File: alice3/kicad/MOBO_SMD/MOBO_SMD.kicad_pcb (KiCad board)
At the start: 2 copper layers, 90.2 x 48.3 mm, 64 parts, among them CON1 MicroSD, J1 VGA, P1 CONN_01X05, P2 USB_OTG, P3 UART1, SW1 RESET, SW2 SOFT RESET, SW3 FLASH ARM, U1 Z80CPU-SMD, U2 Propeller_P8X32A-Q44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

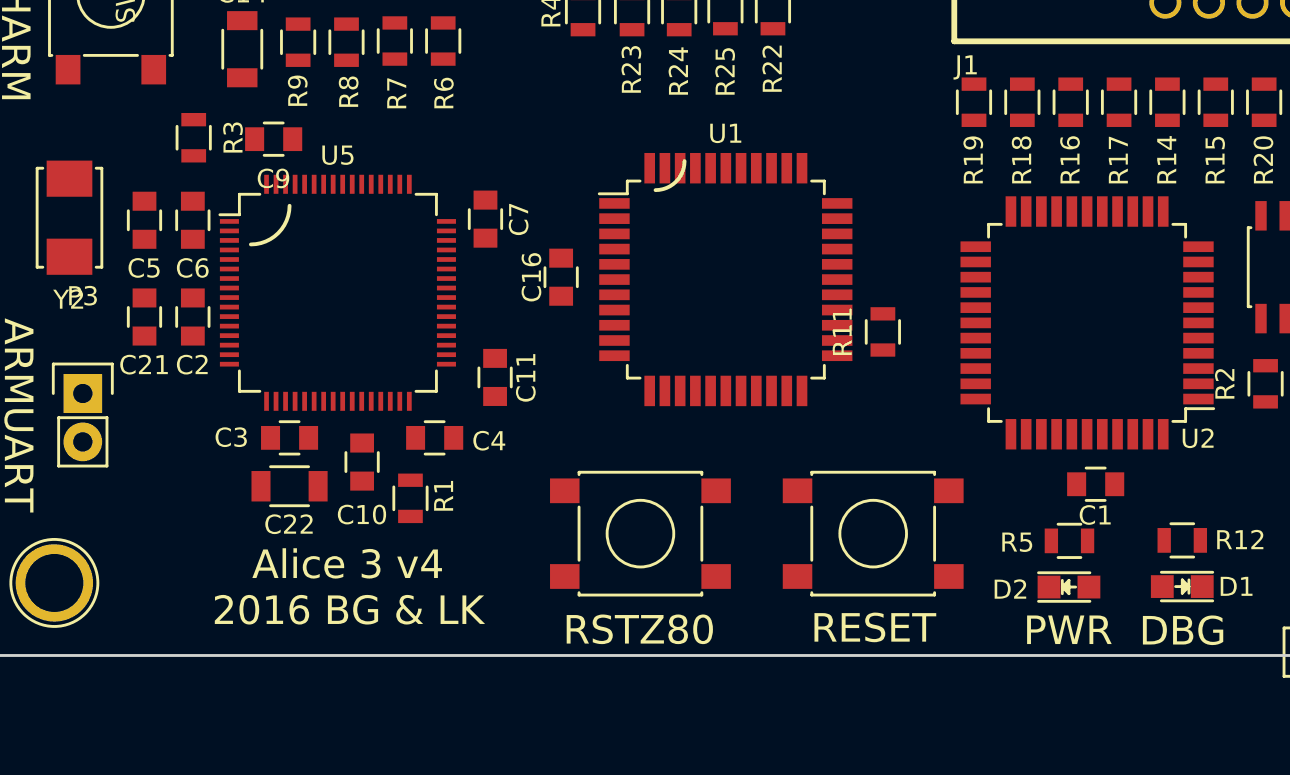
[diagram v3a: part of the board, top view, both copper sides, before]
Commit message: Fix microUSB and mounting holes
Fix footprint for microUSB

Give references for mounting holes
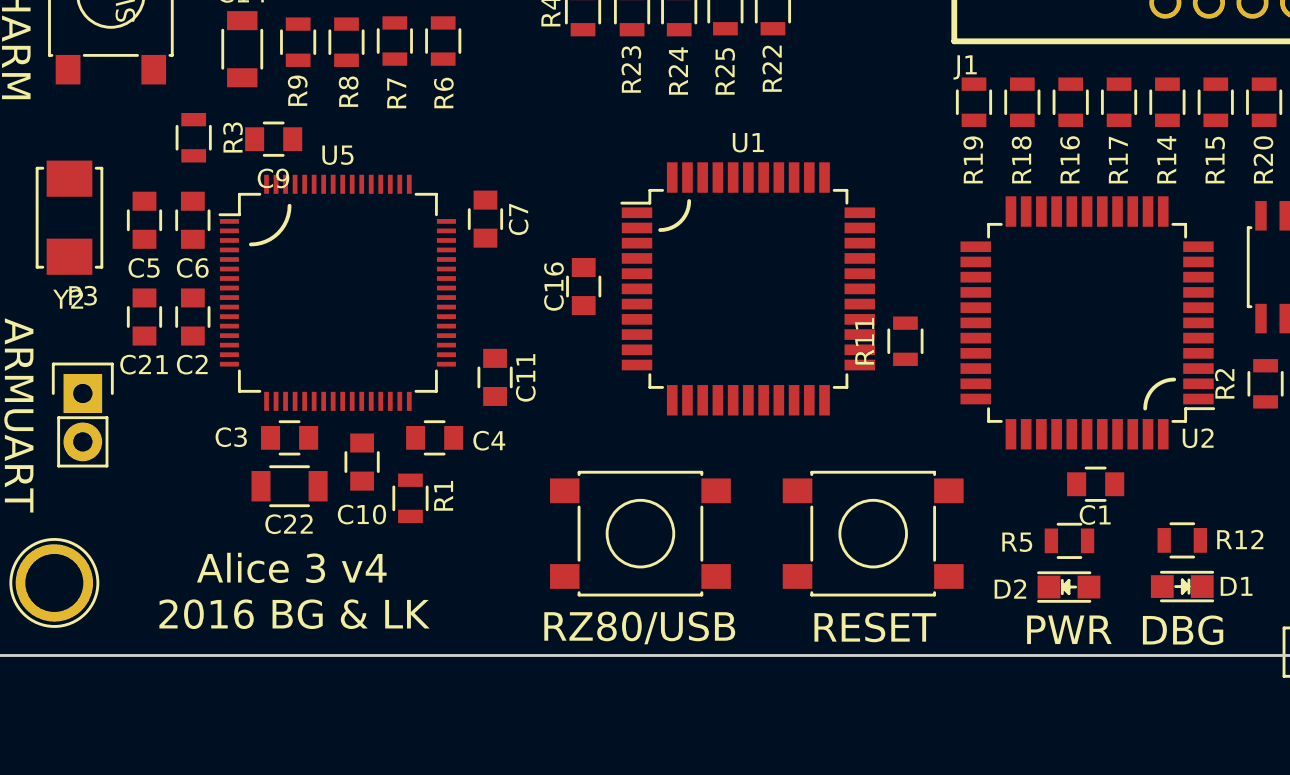
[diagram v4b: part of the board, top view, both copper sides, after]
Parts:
- moved C16 1.28 mm to (140.8, 102.5)
- moved R11 1.28 mm to (157.7, 105.4)
- moved U1 1.28 mm to (149.5, 102.7)
- renumbered REF** to HOLE0, REF** to HOLE1, REF** to HOLE2, REF** to HOLE3
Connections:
- U5 pad 10: ~WR -> A2
- U5 pad 11: A15 -> A3
- U5 pad 2: A10 -> A13
- U5 pad 24: A7 -> A4
- U5 pad 25: A2 -> A5
- U5 pad 26: ~Z80_RESET -> ~IORQ
- U5 pad 29: A4 -> ~BUSRQ
- U5 pad 3: ~PROP_READY~ -> A14
- U5 pad 37: A14 -> A6
- U5 pad 38: A13 -> A7
- U5 pad 39: A12 -> A8
- U5 pad 4: ~RFSH -> A15
- U5 pad 40: A8 -> A9
- U5 pad 46: A1 -> ~PROP_READY~
- U5 pad 49: A0 -> ~RFSH
- U5 pad 51: ~BUSACK -> A10
- U5 pad 52: ~BUSRQ -> A11
- U5 pad 53: A11 -> A12
- U5 pad 55: A3 -> ~RD
- U5 pad 56: A9 -> ~WR
- U5 pad 61: A6 -> ~Z80_RESET
- U5 pad 62: A5 -> ~BUSACK
- U5 pad 8: ~IORQ -> A0
- U5 pad 9: ~RD -> A1
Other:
- board text added: "RZ80/USB"
- board text removed: "RSTZ80"
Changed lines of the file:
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@@
 (kicad_pcb (version 4) (host pcbnew 4.0.6)
   (general
-    (links 218)
-    (no_connects 218)
+    (links 220)
+    (no_connects 220)
     (area 109.144999 73.584999 199.465001 121.995001)
     (thickness 1.6)
-    (drawings 16)
+    (drawings 17)
     (tracks 0)
     (zones 0)
@@
   )
   (module Housings_QFP:LQFP-44_10x10mm_Pitch0.8mm (layer F.Cu)
-    (at 148.3 102.175)
+    (at 149.484423 102.664503)
     (descr "LQFP44 (see Appnote_PCB_Guidelines_TRINAMIC_packages.pdf)")
     (tags "QFP 0.8")
@@
   )
   (module Capacitors_SMD:C_0805 (layer F.Cu)
-    (at 139.65 102.05 270)
+    (at 140.834423 102.539503 270)
     (descr "Capacitor SMD 0805, reflow soldering, AVX (see smccp.pdf)")
     (tags "capacitor 0805")
@@
   )
   (module Resistors_SMD:R_0805 (layer F.Cu)
-    (at 156.55 104.925 90)
+    (at 157.734423 105.414503 90)
     (descr "Resistor SMD 0805, reflow soldering, Vishay (see dcrcw.pdf)")
     (tags "resistor 0805")
@@
     (descr "module 1 pin (ou trou mecanique de percage)")
     (tags DEV)
-    (fp_text reference REF** (at 0 -3.048) (layer F.SilkS) hide
+    (fp_text reference HOLE0 (at 0 -3.048) (layer F.SilkS) hide
       (effects (font (size 1 1) (thickness 0.15)))
     )
@@
     (descr "module 1 pin (ou trou mecanique de percage)")
     (tags DEV)
-    (fp_text reference REF** (at 0 -3.048) (layer F.SilkS) hide
+    (fp_text reference HOLE1 (at 0 -3.048) (layer F.SilkS) hide
       (effects (font (size 1 1) (thickness 0.15)))
     )
@@
     (descr "module 1 pin (ou trou mecanique de percage)")
     (tags DEV)
-    (fp_text reference REF** (at 0 -3.048) (layer F.SilkS) hide
+    (fp_text reference HOLE2 (at 0 -3.048) (layer F.SilkS) hide
       (effects (font (size 1 1) (thickness 0.15)))
     )
@@
       (net 1 +3V3))
     (pad 2 smd rect (at -5.7 -3.25) (size 1 0.25) (layers F.Cu F.Paste F.Mask)
-      (net 42 A10))
+      (net 46 A13))
     (pad 3 smd rect (at -5.7 -2.75) (size 1 0.25) (layers F.Cu F.Paste F.Mask)
-      (net 85 ~PROP_READY~))
+      (net 45 A14))
     (pad 4 smd rect (at -5.7 -2.25) (size 1 0.25) (layers F.Cu F.Paste F.Mask)
-      (net 99 ~RFSH))
+      (net 43 A15))
     (pad 5 smd rect (at -5.7 -1.75) (size 1 0.25) (layers F.Cu F.Paste F.Mask)
       (net 3 "Net-(C5-Pad1)"))
@@
       (net 90 ~RESET))
     (pad 8 smd rect (at -5.7 -0.25) (size 1 0.25) (layers F.Cu F.Paste F.Mask)
-      (net 93 ~IORQ))
+      (net 38 A0))
     (pad 9 smd rect (at -5.7 0.25) (size 1 0.25) (layers F.Cu F.Paste F.Mask)
-      (net 94 ~RD))
+      (net 39 A1))
     (pad 10 smd rect (at -5.7 0.75) (size 1 0.25) (layers F.Cu F.Paste F.Mask)
-      (net 95 ~WR))
+      (net 40 A2))
     (pad 11 smd rect (at -5.7 1.25) (size 1 0.25) (layers F.Cu F.Paste F.Mask)
-      (net 43 A15))
+      (net 50 A3))
     (pad 12 smd rect (at -5.7 1.75) (size 1 0.25) (layers F.Cu F.Paste F.Mask)
       (net 2 GND))
@@
       (net 37 D7))
     (pad 24 smd rect (at -0.25 5.7 90) (size 1 0.25) (layers F.Cu F.Paste F.Mask)
-      (net 28 A7))
+      (net 44 A4))
     (pad 25 smd rect (at 0.25 5.7 90) (size 1 0.25) (layers F.Cu F.Paste F.Mask)
-      (net 40 A2))
+      (net 53 A5))
     (pad 26 smd rect (at 0.75 5.7 90) (size 1 0.25) (layers F.Cu F.Paste F.Mask)
-      (net 89 ~Z80_RESET))
+      (net 93 ~IORQ))
     (pad 27 smd rect (at 1.25 5.7 90) (size 1 0.25) (layers F.Cu F.Paste F.Mask)
       (net 92 ~MREQ))
@@
       (net 64 "Net-(R1-Pad1)"))
     (pad 29 smd rect (at 2.25 5.7 90) (size 1 0.25) (layers F.Cu F.Paste F.Mask)
-      (net 44 A4))
+      (net 98 ~BUSRQ))
     (pad 30 smd rect (at 2.75 5.7 90) (size 1 0.25) (layers F.Cu F.Paste F.Mask)
       (net 27 KBD_CLK))
@@
       (net 11 /IO/DI))
     (pad 37 smd rect (at 5.7 1.75) (size 1 0.25) (layers F.Cu F.Paste F.Mask)
-      (net 45 A14))
+      (net 52 A6))
     (pad 38 smd rect (at 5.7 1.25) (size 1 0.25) (layers F.Cu F.Paste F.Mask)
-      (net 46 A13))
+      (net 28 A7))
     (pad 39 smd rect (at 5.7 0.75) (size 1 0.25) (layers F.Cu F.Paste F.Mask)
-      (net 47 A12))
+      (net 48 A8))
     (pad 40 smd rect (at 5.7 0.25) (size 1 0.25) (layers F.Cu F.Paste F.Mask)
-      (net 48 A8))
+      (net 51 A9))
     (pad 41 smd rect (at 5.7 -0.25) (size 1 0.25) (layers F.Cu F.Paste F.Mask)
       (net 12 /IO/CS))
@@
       (net 20 USB_D_P))
     (pad 46 smd rect (at 5.7 -2.75) (size 1 0.25) (layers F.Cu F.Paste F.Mask)
-      (net 39 A1))
+      (net 85 ~PROP_READY~))
     (pad 47 smd rect (at 5.7 -3.25) (size 1 0.25) (layers F.Cu F.Paste F.Mask)
       (net 7 "Net-(C11-Pad1)"))
@@
       (net 1 +3V3))
     (pad 49 smd rect (at 3.75 -5.7 90) (size 1 0.25) (layers F.Cu F.Paste F.Mask)
-      (net 38 A0))
+      (net 99 ~RFSH))
     (pad 50 smd rect (at 3.25 -5.7 90) (size 1 0.25) (layers F.Cu F.Paste F.Mask)
       (net 91 ~HALT))
     (pad 51 smd rect (at 2.75 -5.7 90) (size 1 0.25) (layers F.Cu F.Paste F.Mask)
-      (net 96 ~BUSACK))
+      (net 42 A10))
     (pad 52 smd rect (at 2.25 -5.7 90) (size 1 0.25) (layers F.Cu F.Paste F.Mask)
-      (net 98 ~BUSRQ))
+      (net 49 A11))
     (pad 53 smd rect (at 1.75 -5.7 90) (size 1 0.25) (layers F.Cu F.Paste F.Mask)
-      (net 49 A11))
+      (net 47 A12))
     (pad 54 smd rect (at 1.25 -5.7 90) (size 1 0.25) (layers F.Cu F.Paste F.Mask)
       (net 97 ~WAIT))
     (pad 55 smd rect (at 0.75 -5.7 90) (size 1 0.25) (layers F.Cu F.Paste F.Mask)
-      (net 50 A3))
+      (net 94 ~RD))
     (pad 56 smd rect (at 0.25 -5.7 90) (size 1 0.25) (layers F.Cu F.Paste F.Mask)
-      (net 51 A9))
+      (net 95 ~WR))
     (pad 57 smd rect (at -0.25 -5.7 90) (size 1 0.25) (layers F.Cu F.Paste F.Mask)
       (net 75 "Net-(SW2-Pad1)"))
@@
       (net 88 "Net-(R3-Pad1)"))
     (pad 61 smd rect (at -2.25 -5.7 90) (size 1 0.25) (layers F.Cu F.Paste F.Mask)
-      (net 52 A6))
+      (net 89 ~Z80_RESET))
     (pad 62 smd rect (at -2.75 -5.7 90) (size 1 0.25) (layers F.Cu F.Paste F.Mask)
-      (net 53 A5))
+      (net 96 ~BUSACK))
     (pad 63 smd rect (at -3.25 -5.7 90) (size 1 0.25) (layers F.Cu F.Paste F.Mask)
       (net 2 GND))
@@
     (descr "module 1 pin (ou trou mecanique de percage)")
     (tags DEV)
-    (fp_text reference REF** (at 0 -3.048) (layer F.SilkS) hide
+    (fp_text reference HOLE3 (at 0 -3.048) (layer F.SilkS) hide
       (effects (font (size 1 1) (thickness 0.15)))
     )
@@
     (pad M2 smd rect (at 1.2 -1.45 90) (size 1.9 1.9) (layers F.Cu F.Paste F.Mask)
       (solder_mask_margin 0.2))
-    (pad S1 smd rect (at -3.85 -1.45 90) (size 1.9 1.9) (layers F.Cu F.Paste F.Mask)
-      (solder_mask_margin 0.2))
-    (pad S3 smd rect (at -3.1 -4 90) (size 2.1 1.6) (layers F.Cu F.Paste F.Mask)
-      (solder_mask_margin 0.2))
-    (pad S4 smd rect (at 3.1 -4 90) (size 2.1 1.6) (layers F.Cu F.Paste F.Mask)
-      (solder_mask_margin 0.2))
-    (pad S2 smd rect (at 3.85 -1.45 90) (size 1.9 1.9) (layers F.Cu F.Paste F.Mask)
-      (solder_mask_margin 0.2))
-  )
+    (pad 6 smd rect (at -3.85 -1.45 90) (size 1.9 1.9) (layers F.Cu F.Paste F.Mask)
+      (net 2 GND) (solder_mask_margin 0.2))
+    (pad 6 smd rect (at -3.1 -4 90) (size 2.1 1.6) (layers F.Cu F.Paste F.Mask)
+      (net 2 GND) (solder_mask_margin 0.2))
+    (pad 6 smd rect (at 3.1 -4 90) (size 2.1 1.6) (layers F.Cu F.Paste F.Mask)
+      (net 2 GND) (solder_mask_margin 0.2))
+    (pad 6 smd rect (at 3.85 -1.45 90) (size 1.9 1.9) (layers F.Cu F.Paste F.Mask)
+      (net 2 GND) (solder_mask_margin 0.2))
+  )
+  (gr_arc (start 171.85 108.949) (end 170.326 108.949) (angle 90) (layer F.SilkS) (width 0.2))
   (gr_text BARTCONN (at 184.2 115.925) (layer F.SilkS)
     (effects (font (size 1.5 1.5) (thickness 0.3)))
@@
     (effects (font (size 1.5 1.5) (thickness 0.3)))
   )
-  (gr_text RSTZ80 (at 143.75 120.6) (layer F.SilkS)
+  (gr_text RZ80/USB (at 143.75 120.45) (layer F.SilkS)
     (effects (font (size 1.5 1.5) (thickness 0.3)))
   )
@@
   )
   (gr_arc (start 123.353 98.298) (end 125.385 98.298) (angle 90) (layer F.SilkS) (width 0.2))
-  (gr_arc (start 144.608 95.953) (end 146.132 95.953) (angle 90) (layer F.SilkS) (width 0.2))
+  (gr_arc (start 144.851 98.05) (end 146.375 98.05) (angle 90) (layer F.SilkS) (width 0.2))
   (gr_text "Alice 3 Z80/Propeller/ARM v3\nlawrence.kesteloot@gmail.com\ngrantham@plunk.org\nhttp://plunk.org/alice3" (at 155.956 102.616) (layer B.SilkS)
     (effects (font (size 1.5 1.5) (thickness 0.3)) (justify mirror))
   )
-  (gr_text "Alice 3 v4\n2016 BG & LK" (at 128.46 118.364) (layer F.SilkS)
+  (gr_text "Alice 3 v4\n2016 BG & LK" (at 125.55 118.6) (layer F.SilkS)
     (effects (font (size 1.5 1.5) (thickness 0.3)))
   )

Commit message: fix inductor, fix HOME
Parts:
- moved P1 17.6 mm to (196.6, 103.1), turned to 0 degrees
- moved U4 17.5 mm to (187.2, 119.0), turned to 270 degrees
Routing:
- net GND: track 0.00 -> 300.0 mm, vias 0 -> 3
- net +3V3: track 0.00 -> 30.6 mm
- net /IO/CS: track 0.00 -> 14.7 mm
- net /IO/SCK: track 0.00 -> 14.2 mm
- net /IO/DO: track 0.00 -> 14.2 mm
- net /IO/DI: track 0.00 -> 14.1 mm
- net Net-(R3-Pad1): track 0.00 -> 3.49 mm
- added copper zone on F.Cu, net +3V3
- added copper zone on B.Cu, net GND
